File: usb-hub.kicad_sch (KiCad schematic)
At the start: 7 parts, among them J101 Barrel_Jack, P101 USB_C_Plug_USB2.0, U101 SRV05-4

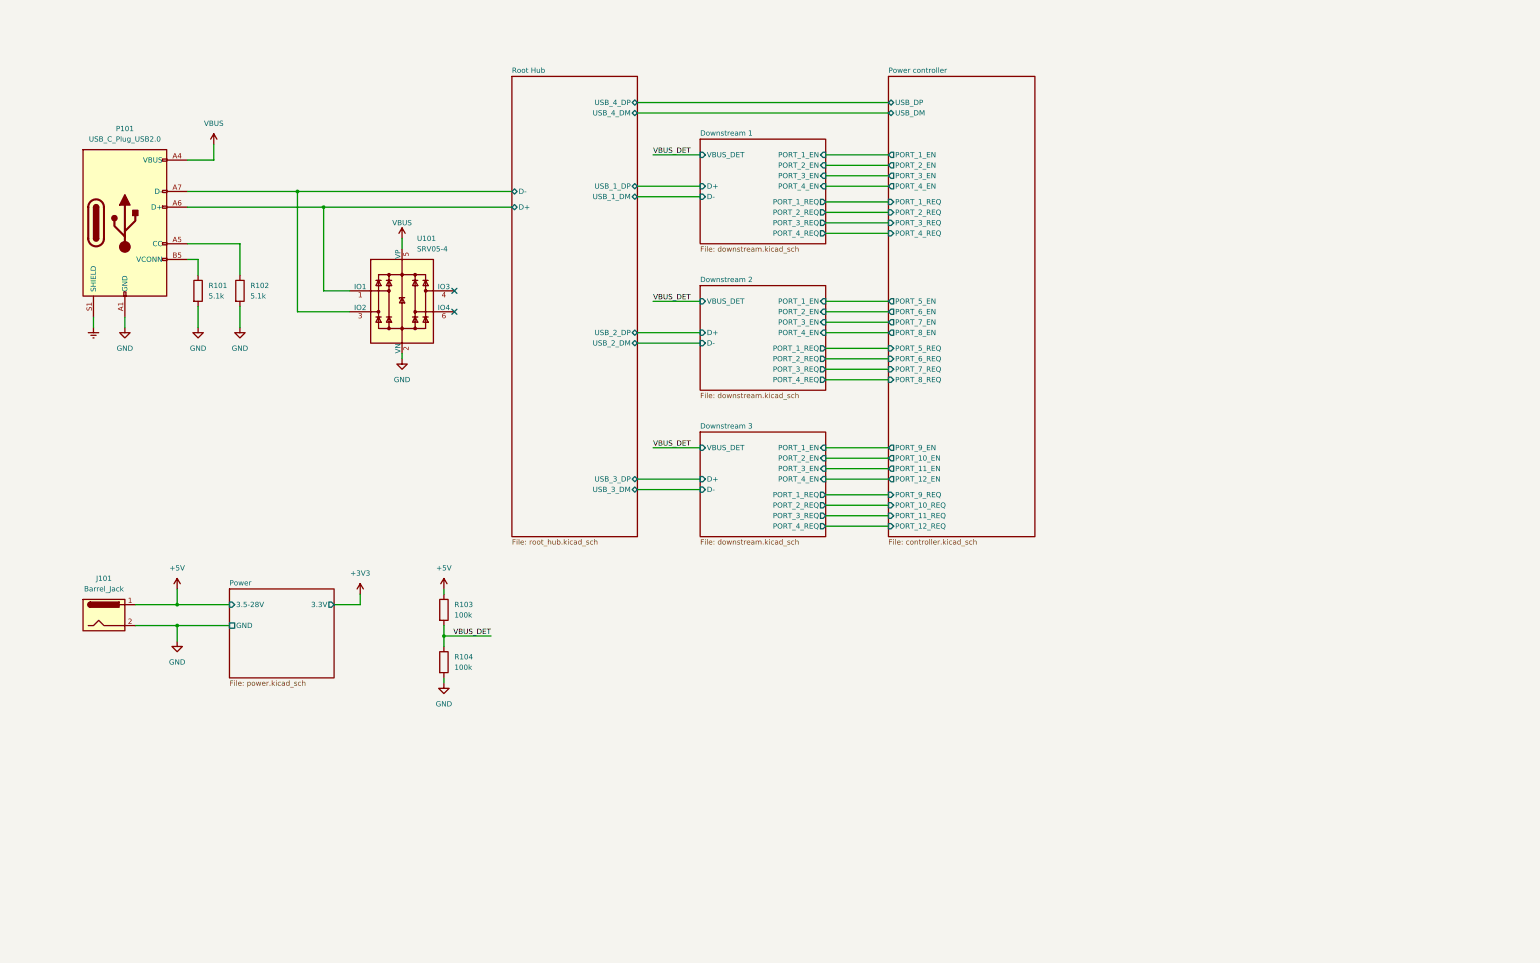
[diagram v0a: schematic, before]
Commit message: Add power management
And also some random stuff here and there
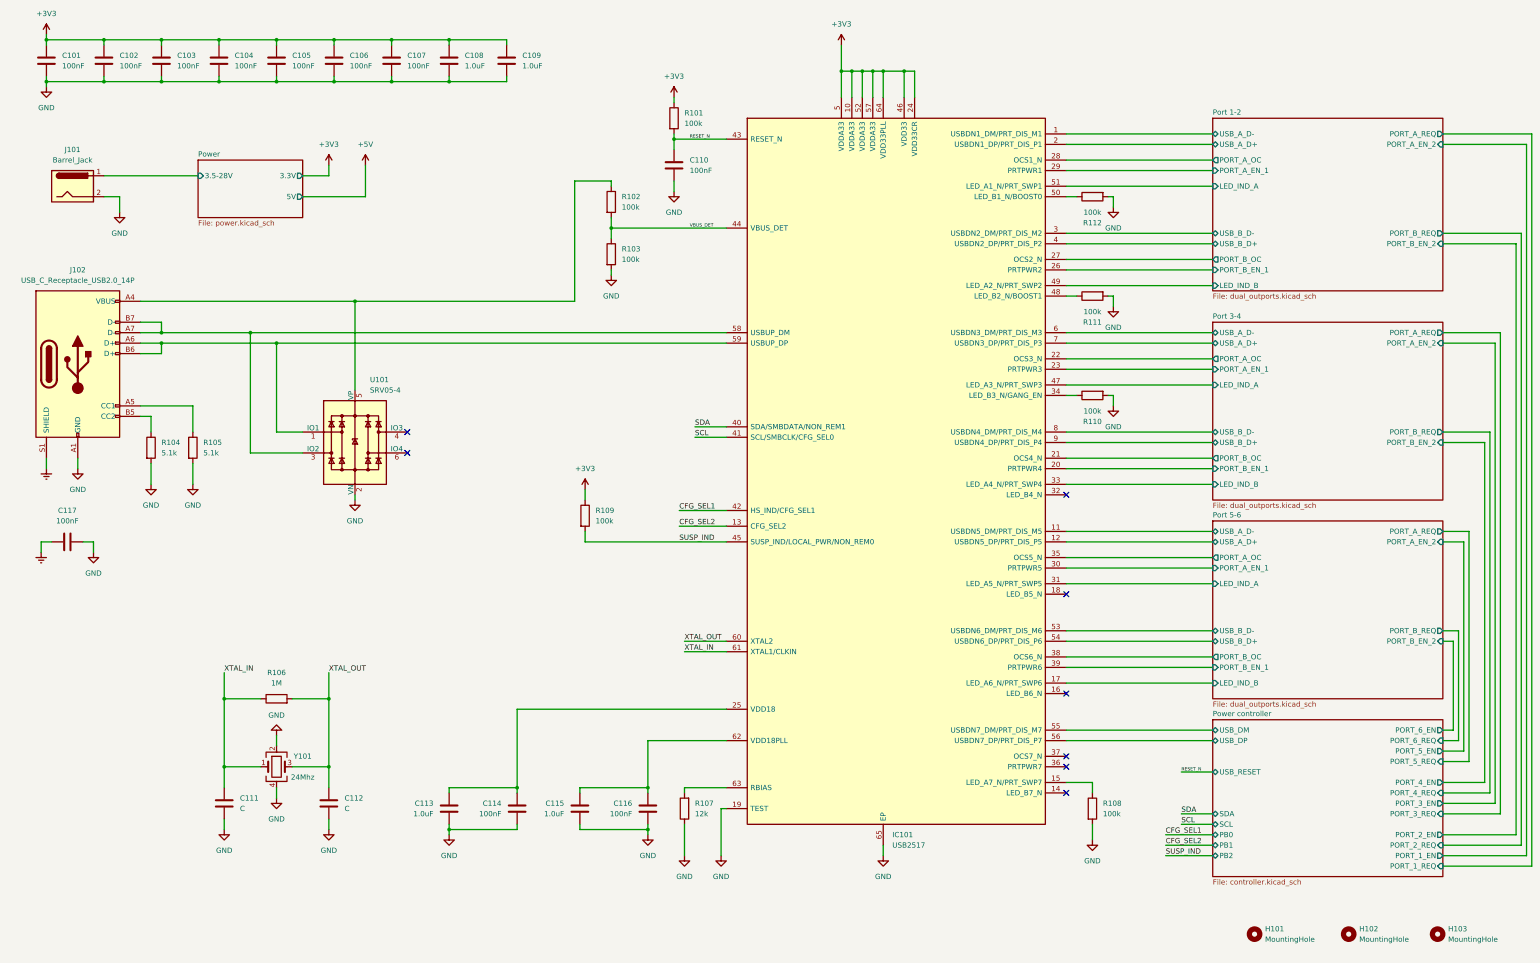
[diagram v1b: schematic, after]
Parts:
- removed P101: USB_C_Plug_USB2.0, Connector_USB:USB_C_Receptacle_G-Switch_GT-USB-7010ASV, symbol Connector:USB_C_Plug_USB2.0
- added C101, C102, C103, C104, C105, C106, C107, C110, C114, C116, C117: 100nF, Capacitor_SMD:C_0402_1005Metric, symbol Device:C
- added C108, C109: 1.0uF, Capacitor_SMD:C_0402_1005Metric, symbol Device:C
- added C111, C112: C, Capacitor_SMD:C_0402_1005Metric, symbol Device:C
- added C113, C115: 1.0uF, Capacitor_SMD:C_0603_1608Metric, symbol Device:C
- added H101, H102, H103: MountingHole, MountingHole:MountingHole_3.2mm_M3, symbol Mechanical:MountingHole
- added IC101: USB2517, Package_DFN_QFN:QFN-64-1EP_9x9mm_P0.5mm_EP4.7x4.7mm_ThermalVias, symbol fabian_usb:USB2517
- added J102: USB_C_Receptacle_USB2.0_14P, Connector_USB:USB_C_Receptacle_XKB_U262-16XN-4BVC11, symbol Connector:USB_C_Receptacle_USB2.0_14P
- added R105: 5.1k, Resistor_SMD:R_0402_1005Metric, symbol Device:R
- added R106: 1M, Resistor_SMD:R_0402_1005Metric, symbol Device:R
- added R107: 12k, Resistor_SMD:R_0402_1005Metric, symbol Device:R
- added R108, R109, R110, R111, R112: 100k, Resistor_SMD:R_0402_1005Metric, symbol Device:R
- added Y101: 24Mhz, Crystal:Crystal_SMD_3225-4Pin_3.2x2.5mm, symbol Device:Crystal_GND24
- J101: footprint Capacitor_SMD:C_0603_1608Metric -> Connector_BarrelJack:BarrelJack_Horizontal
- R101, R102: value 5.1k -> 100k
- R104: value 100k -> 5.1k
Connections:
- net VBUS is gone; now on an unnamed net: U101.5 (VP)
- net +3V3: now also R101.1, C101.1, C102.1, C103.1, C104.1, C105.1, C106.1, C107.1, C108.1, C109.1, IC101.10 (VDDA33), IC101.24 (VDD33CR), IC101.46 (VDD33), IC101.5 (VDDA33), IC101.52 (VDDA33), IC101.57 (VDDA33), IC101.64 (VDD33PLL), R109.1
- net +5V: no longer J101.1, R103.1
- net Earth: now also C117.2, J102.S1 (SHIELD)
- net GND: now also R103.2, C101.2, C102.2, C103.2, C104.2, C105.2, C106.2, C107.2, C108.2, C109.2, C110.2, C111.2, C112.2, C113.2, C114.2, C115.2, C116.2, C117.1, IC101.19 (TEST), IC101.65 (EP), J102.A1 (GND), J102.A12 (GND), J102.B1 (GND), J102.B12 (GND), R105.2, R107.1, R108.2, R110.2, R111.2, R112.2, Y101.2, Y101.4; no longer R101.2, R102.2
- net Power controller/USB_DM: now also IC101.55 (USBDN7_DM/PRT_DIS_M7)
- net Power controller/USB_DP: now also IC101.56 (USBDN7_DP/PRT_DIS_P7)
- net VBUS_DET: now also R102.2, R103.1, IC101.44 (VBUS_DET); no longer R103.2, R104.1
- net at R102.1: now also J102.A4 (VBUS), J102.A9 (VBUS), J102.B4 (VBUS), J102.B9 (VBUS)
- net Root Hub/D+: no longer names the net of U101.1 (IO1)
- net Root Hub/D+: now also IC101.59 (USBUP_DP), J102.A6 (D+), J102.B6 (D+)
- net Root Hub/D-: no longer names the net of U101.3 (IO2)
- net Root Hub/D-: now also IC101.58 (USBUP_DM), J102.A7 (D-), J102.B7 (D-)
- new net: IC101.50 (LED_B1_N/BOOST0), R112.1
- new net: IC101.63 (RBIAS), R107.2
- new net: J102.A5 (CC1), R105.1
- new net: J102.B5 (CC2), R104.1
- new net: C113.1, C114.1, IC101.25 (VDD18)
- new net: IC101.34 (LED_B3_N/GANG_EN), R110.1
- new net: IC101.15 (LED_A7_N/PRT_SWP7), R108.1
- new net: IC101.48 (LED_B2_N/BOOST1), R111.1
- new net: C115.1, C116.1, IC101.62 (VDD18PLL)
- new net CFG_SEL1: IC101.42 (HS_IND/CFG_SEL1)
- new net CFG_SEL2: IC101.13 (CFG_SEL2)
- new net Port 1-2/LED_IND_A: IC101.51 (LED_A1_N/PRT_SWP1)
- new net Port 1-2/LED_IND_B: IC101.49 (LED_A2_N/PRT_SWP2)
- new net Port 1-2/PORT_A_EN_1: IC101.29 (PRTPWR1)
- new net Port 1-2/PORT_A_OC: IC101.28 (OCS1_N)
- new net Port 1-2/PORT_B_EN_1: IC101.26 (PRTPWR2)
- new net Port 1-2/PORT_B_OC: IC101.27 (OCS2_N)
- new net Port 1-2/USB_A_D+: IC101.2 (USBDN1_DP/PRT_DIS_P1)
- new net Port 1-2/USB_A_D-: IC101.1 (USBDN1_DM/PRT_DIS_M1)
- new net Port 1-2/USB_B_D+: IC101.4 (USBDN2_DP/PRT_DIS_P2)
- new net Port 1-2/USB_B_D-: IC101.3 (USBDN2_DM/PRT_DIS_M2)
- new net Port 3-4/LED_IND_A: IC101.47 (LED_A3_N/PRT_SWP3)
- new net Port 3-4/LED_IND_B: IC101.33 (LED_A4_N/PRT_SWP4)
- new net Port 3-4/PORT_A_EN_1: IC101.23 (PRTPWR3)
- new net Port 3-4/PORT_A_OC: IC101.22 (OCS3_N)
- new net Port 3-4/PORT_B_EN_1: IC101.20 (PRTPWR4)
- new net Port 3-4/PORT_B_OC: IC101.21 (OCS4_N)
- new net Port 3-4/USB_A_D+: IC101.7 (USBDN3_DP/PRT_DIS_P3)
- new net Port 3-4/USB_A_D-: IC101.6 (USBDN3_DM/PRT_DIS_M3)
- new net Port 3-4/USB_B_D+: IC101.9 (USBDN4_DP/PRT_DIS_P4)
- new net Port 3-4/USB_B_D-: IC101.8 (USBDN4_DM/PRT_DIS_M4)
- new net Port 5-6/LED_IND_A: IC101.31 (LED_A5_N/PRT_SWP5)
- new net Port 5-6/LED_IND_B: IC101.17 (LED_A6_N/PRT_SWP6)
- new net Port 5-6/PORT_A_EN_1: IC101.30 (PRTPWR5)
- new net Port 5-6/PORT_A_OC: IC101.35 (OCS5_N)
- new net Port 5-6/PORT_B_EN_1: IC101.39 (PRTPWR6)
- new net Port 5-6/PORT_B_OC: IC101.38 (OCS6_N)
- new net Port 5-6/USB_A_D+: IC101.12 (USBDN5_DP/PRT_DIS_P5)
- new net Port 5-6/USB_A_D-: IC101.11 (USBDN5_DM/PRT_DIS_M5)
- new net Port 5-6/USB_B_D+: IC101.54 (USBDN6_DP/PRT_DIS_P6)
- new net Port 5-6/USB_B_D-: IC101.53 (USBDN6_DM/PRT_DIS_M6)
- new net Power/3.5-28V: J101.1
- new net RESET_N: C110.1, IC101.43 (RESET_N), R101.2
- new net SCL: IC101.41 (SCL/SMBCLK/CFG_SEL0)
- new net SDA: IC101.40 (SDA/SMBDATA/NON_REM1)
- new net SUSP_IND: IC101.45 (SUSP_IND/LOCAL_PWR/NON_REM0), R109.2
- new net XTAL_IN: C111.1, IC101.61 (XTAL1/CLKIN), R106.1, Y101.1
- new net XTAL_OUT: C112.1, IC101.60 (XTAL2), R106.2, Y101.3
- no-connect marks 2 -> 8
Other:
- removed sheet Downstream 1
- removed sheet Downstream 2
- removed sheet Downstream 3
- removed sheet Root Hub
- added sheet Port 1-2 (dual_outports.kicad_sch)
- added sheet Port 3-4 (dual_outports.kicad_sch)
- added sheet Port 5-6 (dual_outports.kicad_sch)
- sheet Power ports: added 5V; removed GND
- sheet Power controller ports: added PB0, PB1, PB2, SCL, SDA, USB_RESET; removed PORT_10_EN, PORT_10_REQ, PORT_11_EN, PORT_11_REQ, PORT_12_EN, PORT_12_REQ, PORT_7_EN, PORT_7_REQ, PORT_8_EN, PORT_8_REQ, PORT_9_EN, PORT_9_REQ

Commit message: Refine connectors and overall shape
Replace USB connectors, because of availability.
Use available barrel jack and USB-C connector instead of generic ones.
Update 3D Models

Refine rough placement of parts and board outline
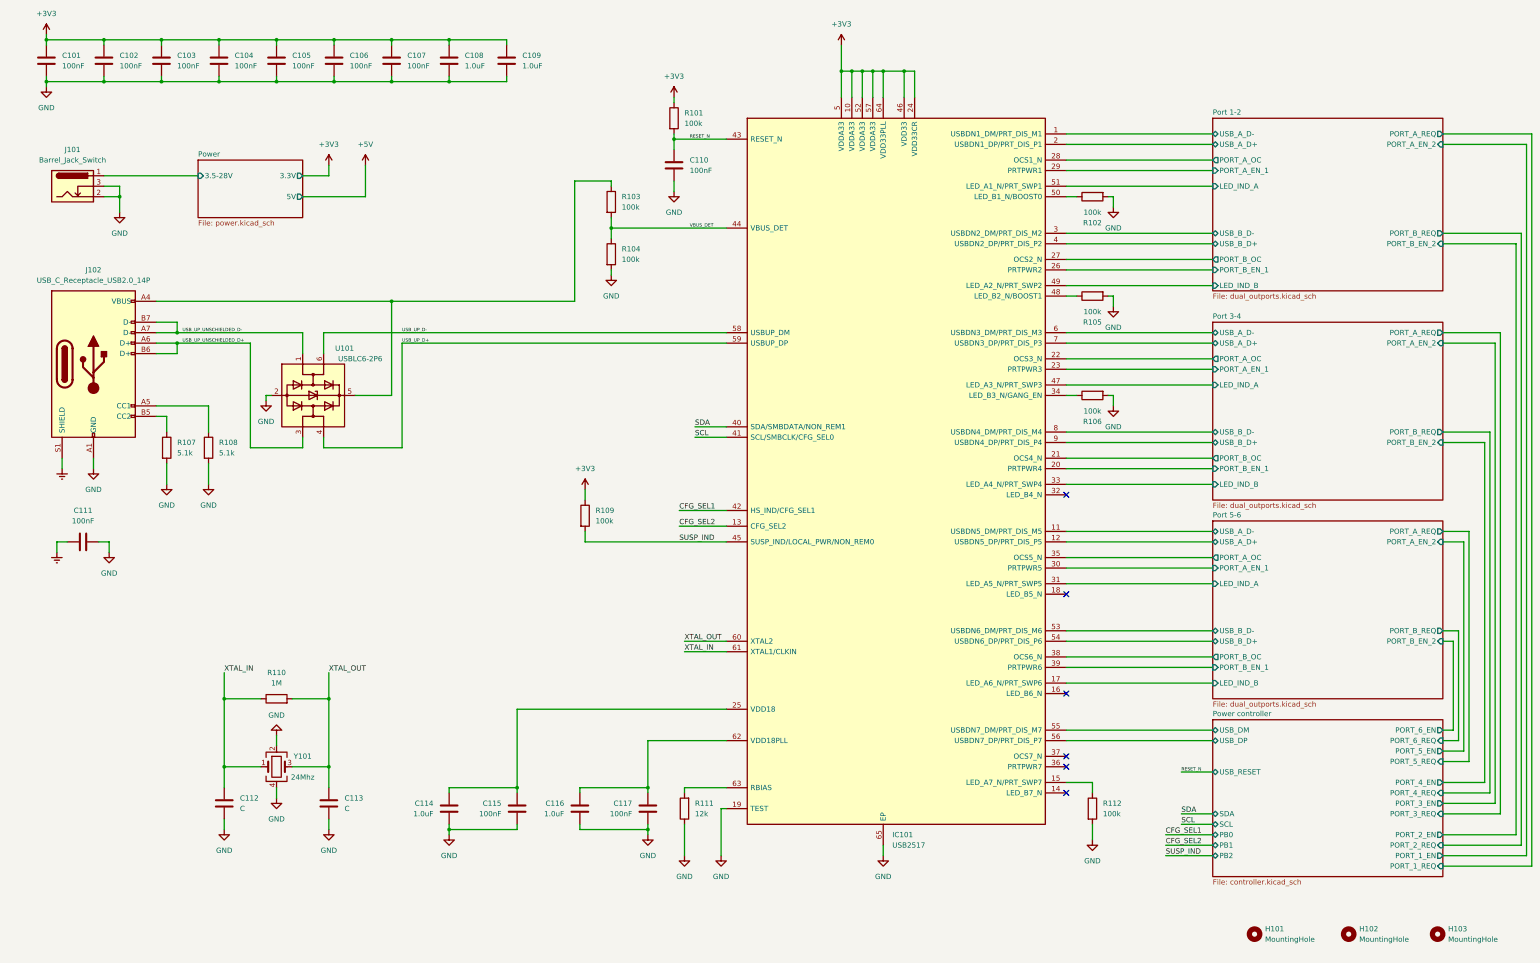
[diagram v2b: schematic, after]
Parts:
- removed J101: Barrel_Jack, Connector_BarrelJack:BarrelJack_Horizontal, symbol Connector:Barrel_Jack
- removed U101: SRV05-4, Package_TO_SOT_SMD:SOT-23-6, symbol Power_Protection:SRV05-4
- added J101: Barrel_Jack_Switch, Connector_BarrelJack:BarrelJack_Wuerth_6941xx301002, symbol Connector:Barrel_Jack_Switch
- added U101: USBLC6-2P6, Package_TO_SOT_SMD:SOT-666, symbol Power_Protection:USBLC6-2P6
- C101, C102, C103, C104, C105, C106, C107, C110: LCSC# (none) -> C307331
- C108, C109: footprint Capacitor_SMD:C_0402_1005Metric -> Capacitor_SMD:C_0603_1608Metric; LCSC# (none) -> C15849
- C111: renamed from C117; LCSC# (none) -> C307331
- C114: renamed from C113; LCSC# (none) -> C15849
- C115: renamed from C114; LCSC# (none) -> C307331
- C116: renamed from C115; LCSC# (none) -> C15849
- C117: renamed from C116; LCSC# (none) -> C307331
- H101, H102, H103: LCSC# (none) -> -
- IC101: LCSC# (none) -> C626668
- J102: footprint Connector_USB:USB_C_Receptacle_XKB_U262-16XN-4BVC11 -> Connector_USB:USB_C_Receptacle_G-Switch_GT-USB-7010ASV; LCSC# (none) -> C2988369
- R101, R109: LCSC# (none) -> C25741; MPN (none) -> 100K
- R102: renamed from R112; LCSC# (none) -> C25741; MPN (none) -> 100K
- R103: renamed from R102; LCSC# (none) -> C25741; MPN (none) -> 100K
- R104: renamed from R103; LCSC# (none) -> C25741; MPN (none) -> 100K
- R105: renamed from R111; LCSC# (none) -> C25741; MPN (none) -> 100K
- R106: renamed from R110; LCSC# (none) -> C25741; MPN (none) -> 100K
- R107: renamed from R104; LCSC# (none) -> C25905; MPN (none) -> 5,1K
- R108: renamed from R105; LCSC# (none) -> C25905; MPN (none) -> 5,1K
- R110: renamed from R106; LCSC# (none) -> C26083; MPN (none) -> 1M
- R111: renamed from R107; LCSC# (none) -> C25752; MPN (none) -> 12K
- R112: renamed from R108; LCSC# (none) -> C25741; MPN (none) -> 100K
- renumbered C111 to C112, C112 to C113
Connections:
- net GND: now also J101.2, J101.3, U101.2 (GND)
- net Power/3.5-28V: now also J101.1
- net at J102.A4 (VBUS), J102.A9 (VBUS), J102.B4 (VBUS)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: now also U101.5 (VBUS)
- net USB_UP_UNSCHIELDED_D+: now reaches J102.A6 (D+), J102.B6 (D+)
- net USB_UP_UNSCHIELDED_D+: now also U101.3 (I/O2); no longer IC101.59 (USBUP_DP)
- net USB_UP_UNSCHIELDED_D-: now reaches J102.A7 (D-), J102.B7 (D-)
- net USB_UP_UNSCHIELDED_D-: now also U101.1 (I/O1); no longer IC101.58 (USBUP_DM)
- new net USB_UP_D+: IC101.59 (USBUP_DP), U101.4 (I/O2)
- new net USB_UP_D-: IC101.58 (USBUP_DM), U101.6 (I/O1)
- no-connect marks 8 -> 6
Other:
- moved on the sheet: C111, J102, R107, R108
